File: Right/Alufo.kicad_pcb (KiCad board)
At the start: 2 copper layers, 139.7 x 88.9 mm, 67 parts, among them J2 USB_C_Receptacle_USB2.0_16P_2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, J4 USB_C_Receptacle_USB2.0_16P_2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, K11 PG1350, K12 PG1350, K13 PG1350, K14 PG1350, K15 PG1350, K16 PG1350, K21 PG1350, K22 PG1350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

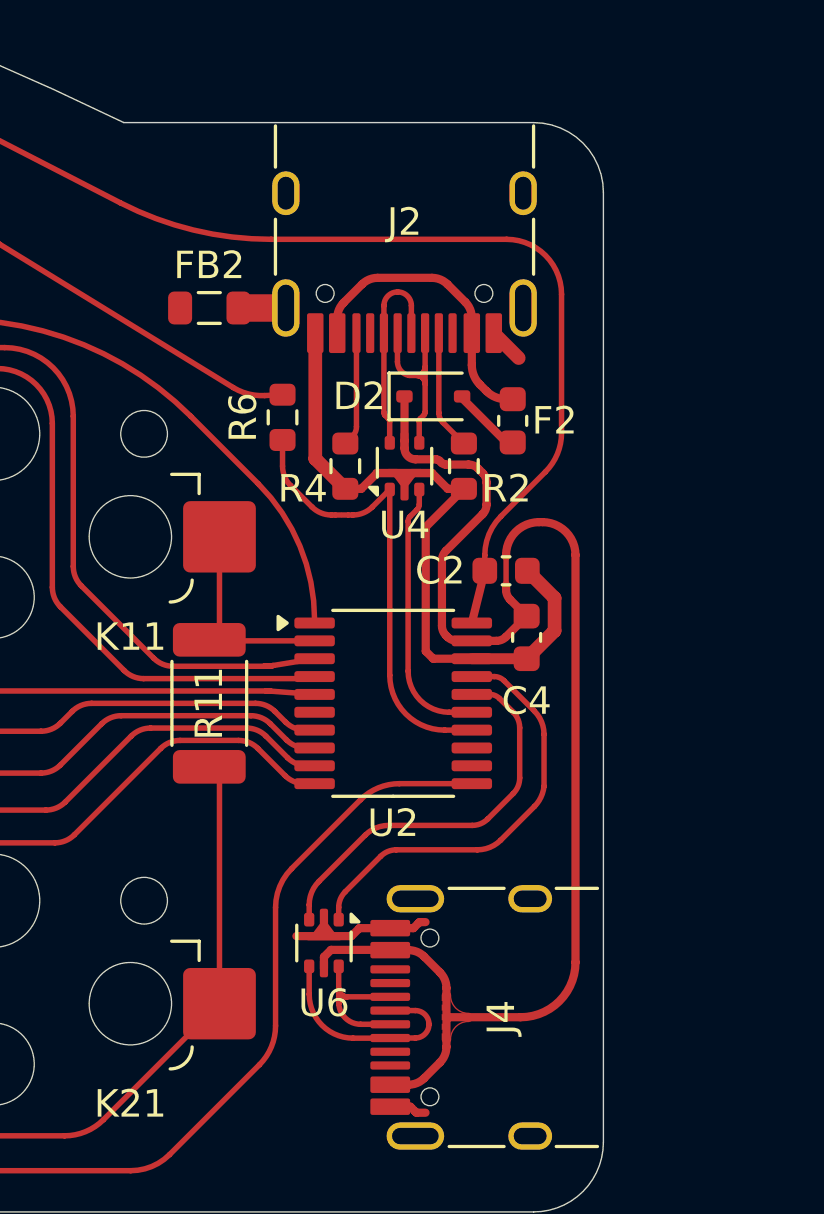
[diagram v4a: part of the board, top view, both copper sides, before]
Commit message: Add order number location
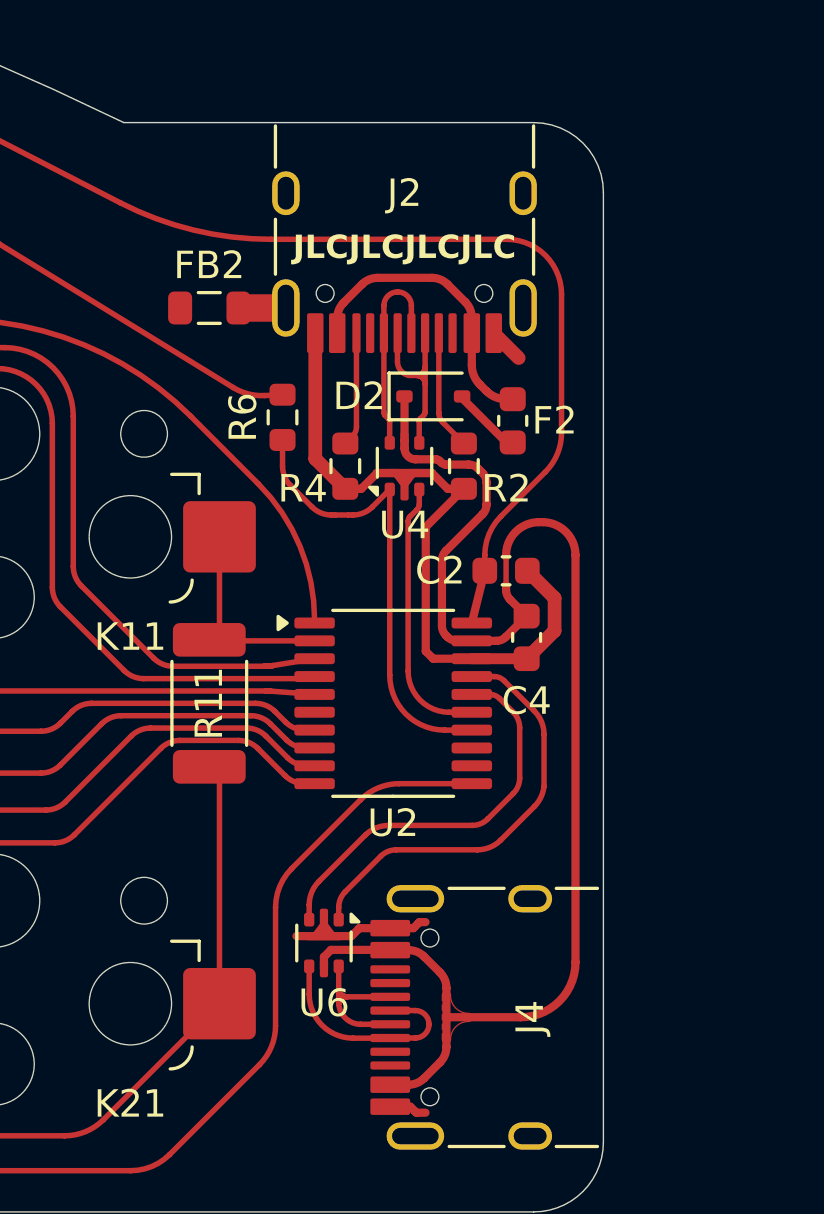
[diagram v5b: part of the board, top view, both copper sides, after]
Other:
- board text added: "JLCJLCJLCJLC"
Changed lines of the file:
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@@
 		(tags "usb usb-c 2.0 pd")
 		(property "Reference" "J2"
-			(at 0 0 180)
+			(at 0 1.05 180)
 			(layer "F.SilkS")
 			(effects
@@
 		)
 		(fp_text user "${REFERENCE}"
-			(at 0 0 180)
+			(at 0 1.05 180)
 			(layer "F.Fab")
 			(effects
@@
 		(tags "usb usb-c 2.0 pd")
 		(property "Reference" "J4"
-			(at 0 0 90)
+			(at 0 1.05 90)
 			(layer "F.SilkS")
 			(effects
@@
 		)
 		(fp_text user "${REFERENCE}"
-			(at 0 0 90)
+			(at 0 1.05 90)
 			(layer "F.Fab")
 			(effects
@@
 		(layer "User.4")
 	)
+	(gr_text "JLCJLCJLCJLC"
+		(at 215.008 45.619 0)
+		(layer "F.SilkS")
+		(effects
+			(font
+				(size 0.85 0.85)
+				(thickness 0.16)
+				(bold yes)
+			)
+		)
+	)
 	(gr_text "${TITLE} v${REVISION}"

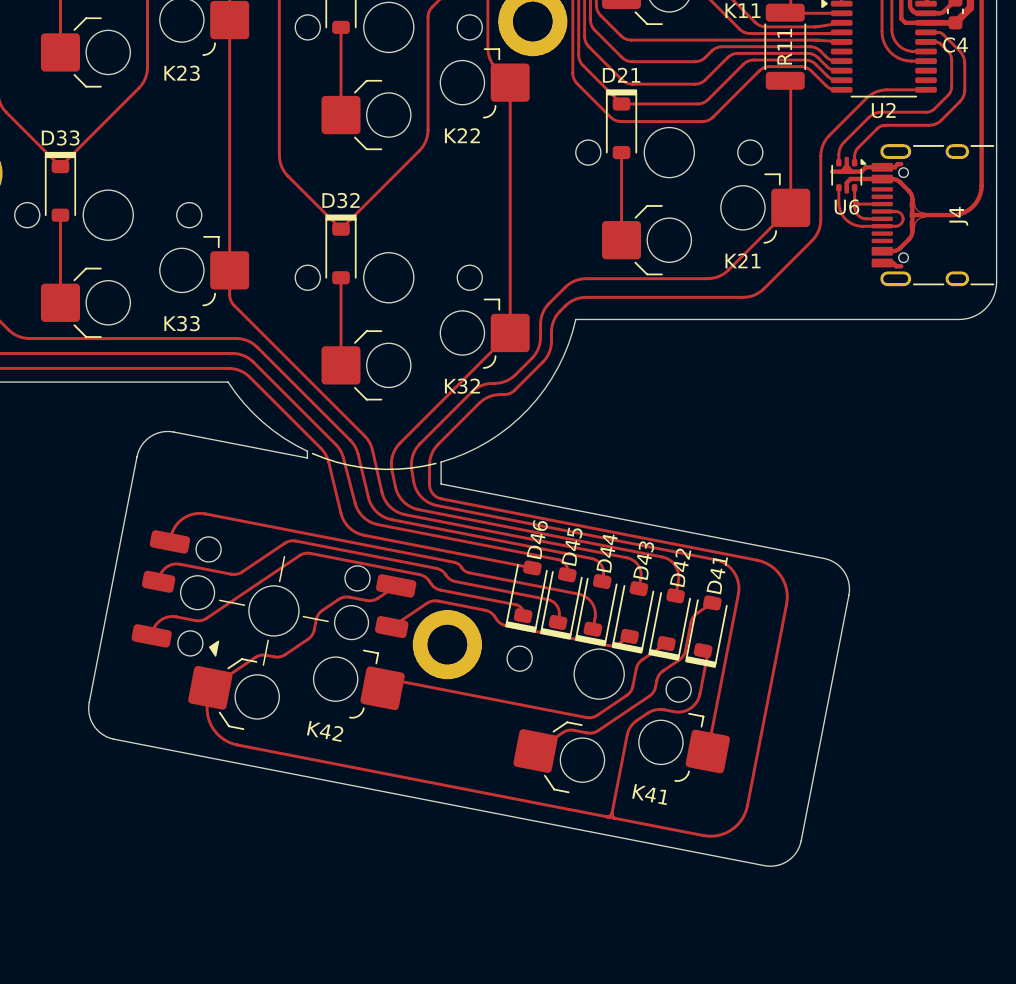
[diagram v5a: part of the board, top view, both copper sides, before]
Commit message: Move thumb clusters down 2mm
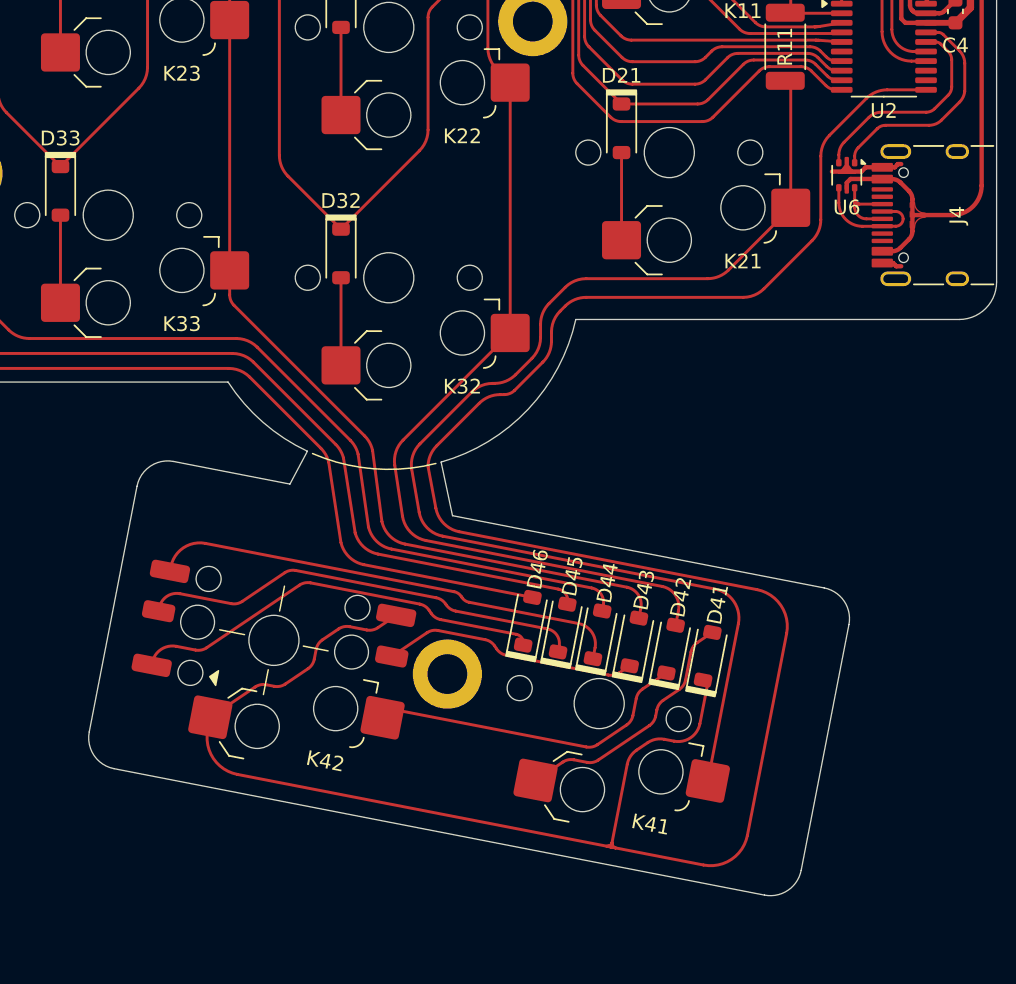
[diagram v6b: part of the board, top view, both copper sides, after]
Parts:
- moved D41 2.00 mm to (202.6, 103.6)
- moved D42 2.00 mm to (200.1, 103.1)
- moved D43 2.00 mm to (197.6, 102.7)
- moved D44 2.00 mm to (195.2, 102.2)
- moved D45 2.00 mm to (192.8, 101.7)
- moved D46 2.00 mm to (190.4, 101.2)
- moved H5 2.00 mm to (185.0, 104.8)
- moved K41 2.00 mm to (195.3, 106.8)
- moved K42 2.00 mm to (173.2, 102.5)
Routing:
- net Col5T: track 92.0 -> 94.0 mm
- net Col3T: track 60.0 -> 62.0 mm
- net Col4T: track 76.1 -> 78.1 mm
- net Col6: track 239.6 -> 241.6 mm
- net Col1T: track 79.6 -> 81.4 mm
- net Col2T: track 60.8 -> 62.4 mm
- net Row4: track 161.3 -> 162.8 mm
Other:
- board size 139.7 x 88.9 mm -> 139.7 x 90.9 mm

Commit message: Add plate to righthand board
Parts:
- added H10: ScrewHole, MountingHole:MountingHole_2.2mm_M2, F.Cu at (270.7, 104.8)
- added H6: ScrewHole, MountingHole:MountingHole_2.2mm_M2, F.Cu at (199.8, 60.5)
- added H7: ScrewHole, MountingHole:MountingHole_2.2mm_M2, F.Cu at (238.1, 48.2)
- added H8: ScrewHole, MountingHole:MountingHole_2.2mm_M2, F.Cu at (238.1, 70.8)
- added H9: ScrewHole, MountingHole:MountingHole_2.2mm_M2, F.Cu at (276.5, 60.5)
- added PK11: SwitchHole, Project Library:SW_choc_v1_Plate_CPG135001S30_1u, F.Cu at (285.7, 52.4)
- added PK12: SwitchHole, Project Library:SW_choc_v1_Plate_CPG135001S30_1u, F.Cu at (266.7, 43.9)
- added PK13: SwitchHole, Project Library:SW_choc_v1_Plate_CPG135001S30_1u, F.Cu at (247.6, 39.7)
- added PK14: SwitchHole, Project Library:SW_choc_v1_Plate_CPG135001S30_1u, F.Cu at (228.6, 39.7)
- added PK15: SwitchHole, Project Library:SW_choc_v1_Plate_CPG135001S30_1u, F.Cu at (209.5, 43.9)
- added PK16: SwitchHole, Project Library:SW_choc_v1_Plate_CPG135001S30_1u, F.Cu at (190.5, 52.4)
- added PK21: SwitchHole, Project Library:SW_choc_v1_Plate_CPG135001S30_1u, F.Cu at (285.7, 69.4)
- added PK22: SwitchHole, Project Library:SW_choc_v1_Plate_CPG135001S30_1u, F.Cu at (266.7, 60.9)
- added PK23: SwitchHole, Project Library:SW_choc_v1_Plate_CPG135001S30_1u, F.Cu at (247.6, 56.7)
- added PK24: SwitchHole, Project Library:SW_choc_v1_Plate_CPG135001S30_1u, F.Cu at (228.6, 56.7)
- added PK25: SwitchHole, Project Library:SW_choc_v1_Plate_CPG135001S30_1u, F.Cu at (209.5, 60.9)
- added PK26: SwitchHole, Project Library:SW_choc_v1_Plate_CPG135001S30_1u, F.Cu at (190.5, 69.4)
- added PK32: SwitchHole, Project Library:SW_choc_v1_Plate_CPG135001S30_1u, F.Cu at (266.7, 77.9)
- added PK33: SwitchHole, Project Library:SW_choc_v1_Plate_CPG135001S30_1u, F.Cu at (247.6, 73.7)
- added PK34: SwitchHole, Project Library:SW_choc_v1_Plate_CPG135001S30_1u, F.Cu at (228.6, 73.7)
- added PK35: SwitchHole, Project Library:SW_choc_v1_Plate_CPG135001S30_1u, F.Cu at (209.5, 77.9)
- added PK41: SwitchHole, Project Library:SW_choc_v1_Plate_CPG135001S30_1.5u, F.Cu at (281.0, 106.8)
- added PK42: SwitchHole, Project Library:SW_choc_v1_Plate_CPG135001S30_1u, F.Cu at (258.9, 102.5)
- H1, H2, H3, H4, H5: value MountingHole -> SolderNut
- moved R8 57.2 mm to (91.8, 33.6)
- moved D11 57.2 mm to (139.6, 50.8)
- moved D13 57.2 mm to (101.5, 39.7)
- moved D2 57.2 mm to (158.9, 51.1)
- moved D21 57.2 mm to (139.6, 67.8)
- moved D23 57.2 mm to (101.5, 56.7)
- moved D33 57.2 mm to (101.5, 72.0)
- moved D41 57.2 mm to (145.5, 103.6)
- moved D42 57.2 mm to (143.0, 103.1)
- moved D43 57.2 mm to (140.5, 102.7)
- moved D44 57.2 mm to (138.0, 102.2)
- moved D45 57.2 mm to (135.6, 101.7)
- moved D46 57.2 mm to (133.3, 101.2)
- moved F2 57.2 mm to (161.8, 51.9)
- moved FB2 57.2 mm to (150.7, 47.8)
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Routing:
- added copper zone on F.Cu, net (none)
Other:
- board size 139.7 x 90.9 mm -> 282.6 x 90.9 mm

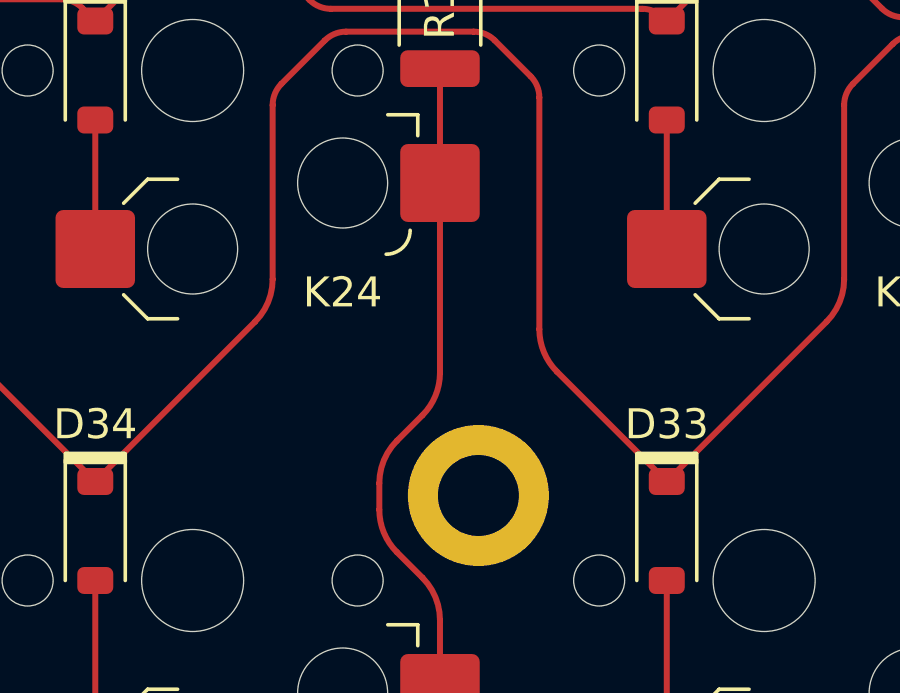
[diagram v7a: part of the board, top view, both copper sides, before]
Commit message: Connect aluminium back to copper layer
Holes J5 and J6 will be filled with solder on the active PCB to connect the back aluminium layer (which is connected to the USB shield) with the mounting hole H3. H3 will in turn connect to the bottom layer PCB via the solder nut pressed against the exposed pad on the active PCB. The solder nut will connect to the screw and the screw will connect to the top plate. The upper middle plate will connect to the shield by virtue of being physically pressed to the active PCB’s back (if correctly oriented).
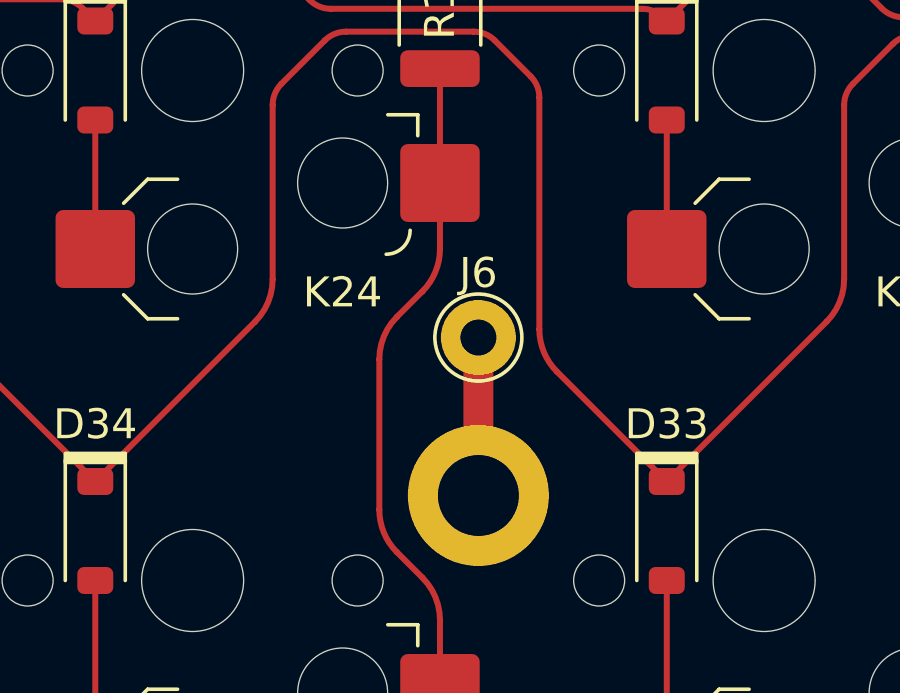
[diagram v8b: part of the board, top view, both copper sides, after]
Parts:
- added J6: SolderHole, TestPoint:TestPoint_THTPad_D2.5mm_Drill1.2mm, F.Cu at (95.2, 65.6)
- H3: footprint Project Library:MountingHole_2.2mm_M2_SMD_Solder_Nut -> Project Library:MountingHole_2.2mm_M2_SMD_Solder_Nut_Pad
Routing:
- net Shield: track 0.00 -> 5.27 mm
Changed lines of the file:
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@@
 	(net 71 "USB+")
 	(net 72 "USB-")
+	(net 73 "Shield")
 	(footprint "Project Library:SW_choc_v1_HS_CPG135001S30_1layer_1u"
 		(layer "F.Cu")
@@
 		)
 	)
-	(footprint "Project Library:MountingHole_2.2mm_M2_SMD_Solder_Nut"
+	(footprint "Project Library:MountingHole_2.2mm_M2_SMD_Solder_Nut_Pad"
 		(layer "F.Cu")
 		(at 95.25 70.83335)
@@
 			)
 		)
-		(property "Footprint" "Project Library:MountingHole_2.2mm_M2_SMD_Solder_Nut"
+		(property "Footprint" "Project Library:MountingHole_2.2mm_M2_SMD_Solder_Nut_Pad"
 			(at 0 0 0)
 			(unlocked yes)
@@
 			)
 		)
-		(property "Description" "Mounting Hole without connection"
+		(property "Description" "Mounting Hole with connection"
 			(at 0 0 0)
 			(unlocked yes)
@@
 			)
 		)
-		(property ki_fp_filters "MountingHole*")
+		(property ki_fp_filters "MountingHole*Pad*")
 		(sheetname "Root")
 		(sheetfile "Alufo.kicad_sch")
@@
 			)
 		)
-		(pad "" thru_hole circle
+		(pad "1" thru_hole circle
 			(at 0 0)
 			(size 4.7 4.7)
@@
 			(layers "*.Cu" "F.Mask")
 			(remove_unused_layers no)
+			(net 73 "Shield")
+			(pinfunction "1")
+			(pintype "input")
+		)
+	)
+	(footprint "TestPoint:TestPoint_THTPad_D2.5mm_Drill1.2mm"
+		(layer "F.Cu")
+		(at 95.25 65.567997)
+		(descr "THT pad as test Point, diameter 2.5mm, hole diameter 1.2mm ")
+		(tags "test point THT pad")
+		(property "Reference" "J6"
+			(at 0 -2.148 0)
+			(layer "F.SilkS")
+			(effects
+				(font
+					(size 1 1)
+					(thickness 0.15)
+				)
+			)
+		)
+		(property "Value" "SolderHole"
+			(at 0 2.25 0)
+			(layer "F.Fab")
+			(effects
+				(font
+					(size 1 1)
+					(thickness 0.15)
+				)
+			)
+		)
+		(property "Footprint" "TestPoint:TestPoint_THTPad_D2.5mm_Drill1.2mm"
+			(at 0 0 0)
+			(unlocked yes)
+			(layer "F.Fab")
+			(hide yes)
+			(effects
+				(font
+					(size 1.27 1.27)
+					(thickness 0.15)
+				)
+			)
+		)
+		(property "Datasheet" ""
+			(at 0 0 0)
+			(unlocked yes)
+			(layer "F.Fab")
+			(hide yes)
+			(effects
+				(font
+					(size 1.27 1.27)
+					(thickness 0.15)
+				)
+			)
+		)
+		(property "Description" "Generic connector, single row, 01x01, script generated"
+			(at 0 0 0)
+			(unlocked yes)
+			(layer "F.Fab")
+			(hide yes)
+			(effects
+				(font
+					(size 1.27 1.27)
+					(thickness 0.15)
+				)
+			)
+		)
+		(property ki_fp_filters "Connector*:*_1x??_*")
+		(sheetname "Root")
+		(sheetfile "Alufo.kicad_sch")
+		(attr exclude_from_pos_files)
+		(fp_circle
+			(center 0 0)
+			(end 0 1.45)
+			(stroke
+				(width 0.12)
+				(type solid)
+			)
+			(fill none)
+			(layer "F.SilkS")
+		)
+		(fp_circle
+			(center 0 0)
+			(end 1.75 0)
+			(stroke
+				(width 0.05)
+				(type solid)
+			)
+			(fill none)
+			(layer "F.CrtYd")
+		)
+		(fp_text user "${REFERENCE}"
+			(at 0 -2.15 0)
+			(layer "F.Fab")
+			(effects
+				(font
+					(size 1 1)
+					(thickness 0.15)
+				)
+			)
+		)
+		(pad "1" thru_hole circle
+			(at 0 0)
+			(size 2.5 2.5)
+			(drill 1.2)
+			(layers "*.Cu" "*.Mask")
+			(remove_unused_layers no)
+			(net 73 "Shield")
+			(pinfunction "Pin_1")
+			(pintype "passive")
 		)
 	)
@@
 	)
 	(segment
+		(start 93.97 62.615173)
+		(end 93.97 60.41668)
+		(width 0.2)
+		(layer "F.Cu")
+		(net 47)
+	)
+	(segment
 		(start 138.317434 100.546183)
 		(end 138.393376 100.155495)
@@
 	)
 	(segment
-		(start 113.471573 82.042)
-		(end 99.423743 82.042)
+		(start 91.948 66.294027)
+		(end 91.948 71.307573)
 		(width 0.2)
 		(layer "F.Cu")
@@
 	)
 	(segment
-		(start 91.948 70.424427)
-		(end 91.948 71.307573)
+		(start 113.471573 82.042)
+		(end 99.423743 82.042)
 		(width 0.2)
 		(layer "F.Cu")
@@
 	)
 	(segment
-		(start 93.384213 68.159787)
-		(end 92.533786 69.010214)
+		(start 93.384213 64.029387)
+		(end 92.533786 64.879814)
 		(width 0.2)
 		(layer "F.Cu")
@@
 	)
 	(segment
-		(start 93.97 60.41668)
-		(end 93.97 66.745573)
-		(width 0.2)
-		(layer "F.Cu")
-		(net 47)
-	)
-	(segment
 		(start 93.97 74.986427)
 		(end 93.97 77.416684)
@@
 	)
 	(arc
-		(start 93.384213 68.159787)
-		(mid 93.817759 67.51094)
-		(end 93.97 66.745573)
+		(start 93.384213 64.029387)
+		(mid 93.817759 63.38054)
+		(end 93.97 62.615173)
 		(width 0.2)
 		(layer "F.Cu")
@@
 	)
 	(arc
-		(start 91.948 70.424427)
-		(mid 92.100241 69.65906)
-		(end 92.533786 69.010214)
+		(start 91.948 66.294027)
+		(mid 92.100241 65.52866)
+		(end 92.533786 64.879814)
 		(width 0.2)
 		(layer "F.Cu")
@@
 		(net 72)
 	)
+	(segment
+		(start 95.25 65.567997)
+		(end 95.25 70.83335)
+		(width 1)
+		(layer "F.Cu")
+		(net 73)
+	)
 	(zone
